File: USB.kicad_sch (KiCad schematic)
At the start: 4 parts, among them J6 USB_B_Micro, U1 MCP2221AxML

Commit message: generated drill and gerber files, updeted a few datasheets
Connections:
- net VBUS: now also J6.1 (VBUS), R3.1, U1.10 (VUSB), U1.16 (VDD)
- net at R3.2, U1.3 (~{RST}): no longer J6.1 (VBUS)
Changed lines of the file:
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@@
+	)
+	(junction
+		(at 121.92 91.44)
+		(diameter 0)
+		(color 0 0 0 0)
 	)
 	(junction
@@
 	)
 	(junction
-		(at 132.08 88.9)
+		(at 63.5 49.53)
 		(diameter 0)
 		(color 0 0 0 0)
@@
 	)
 	(junction
+		(at 146.05 60.96)
+		(diameter 0)
+		(color 0 0 0 0)
+	)
+	(junction
 		(at 63.5 59.69)
 		(diameter 0)
@@
 	(wire
 		(pts
-			(xy 132.08 88.9) (xy 132.08 91.44)
-		)
-		(stroke
-			(width 0)
-			(type default)
-		)
-	)
-	(wire
-		(pts
-			(xy 132.08 83.82) (xy 132.08 88.9)
-		)
-		(stroke
-			(width 0)
-			(type default)
-		)
-	)
-	(wire
-		(pts
 			(xy 63.5 71.12) (xy 63.5 68.58)
 		)
@@
 	(wire
 		(pts
-			(xy 63.5 59.69) (xy 63.5 49.53)
+			(xy 59.69 49.53) (xy 63.5 49.53)
+		)
+		(stroke
+			(width 0)
+			(type default)
+		)
+	)
+	(wire
+		(pts
+			(xy 137.16 60.96) (xy 137.16 95.25)
 		)
 		(stroke
@@
 	(wire
 		(pts
-			(xy 137.16 53.34) (xy 137.16 88.9)
-		)
-		(stroke
-			(width 0)
-			(type default)
-		)
-	)
-	(wire
-		(pts
 			(xy 109.22 73.66) (xy 104.14 73.66)
 		)
@@
 	(wire
 		(pts
+			(xy 137.16 95.25) (xy 121.92 95.25)
+		)
+		(stroke
+			(width 0)
+			(type default)
+		)
+	)
+	(wire
+		(pts
 			(xy 129.54 68.58) (xy 129.54 71.12)
 		)
@@
 	(wire
 		(pts
-			(xy 175.26 53.34) (xy 137.16 53.34)
+			(xy 175.26 60.96) (xy 146.05 60.96)
+		)
+		(stroke
+			(width 0)
+			(type default)
+		)
+	)
+	(wire
+		(pts
+			(xy 132.08 83.82) (xy 132.08 91.44)
+		)
+		(stroke
+			(width 0)
+			(type default)
+		)
+	)
+	(wire
+		(pts
+			(xy 121.92 95.25) (xy 121.92 91.44)
 		)
 		(stroke
@@
 	(wire
 		(pts
-			(xy 123.19 91.44) (xy 118.11 91.44)
+			(xy 123.19 91.44) (xy 121.92 91.44)
+		)
+		(stroke
+			(width 0)
+			(type default)
+		)
+	)
+	(wire
+		(pts
+			(xy 121.92 91.44) (xy 118.11 91.44)
 		)
 		(stroke
@@
 	(wire
 		(pts
+			(xy 66.04 49.53) (xy 63.5 49.53)
+		)
+		(stroke
+			(width 0)
+			(type default)
+		)
+	)
+	(wire
+		(pts
+			(xy 146.05 60.96) (xy 146.05 43.18)
+		)
+		(stroke
+			(width 0)
+			(type default)
+		)
+	)
+	(wire
+		(pts
 			(xy 64.77 67.31) (xy 64.77 69.85)
 		)
@@
 	(wire
 		(pts
-			(xy 175.26 53.34) (xy 175.26 60.96)
-		)
-		(stroke
-			(width 0)
-			(type default)
-		)
-	)
-	(wire
-		(pts
 			(xy 64.77 69.85) (xy 66.04 69.85)
 		)
@@
 	(wire
 		(pts
+			(xy 63.5 49.53) (xy 63.5 59.69)
+		)
+		(stroke
+			(width 0)
+			(type default)
+		)
+	)
+	(wire
+		(pts
 			(xy 63.5 67.31) (xy 64.77 67.31)
 		)
@@
 	(wire
 		(pts
-			(xy 137.16 88.9) (xy 132.08 88.9)
+			(xy 146.05 43.18) (xy 66.04 43.18)
 		)
 		(stroke
@@
 	(wire
 		(pts
+			(xy 146.05 60.96) (xy 137.16 60.96)
+		)
+		(stroke
+			(width 0)
+			(type default)
+		)
+	)
+	(wire
+		(pts
 			(xy 63.5 59.69) (xy 63.5 63.5)
+		)
+		(stroke
+			(width 0)
+			(type default)
+		)
+	)
+	(wire
+		(pts
+			(xy 66.04 43.18) (xy 66.04 49.53)
 		)
 		(stroke
@@
 	(hierarchical_label "VBUS"
 		(shape input)
-		(at 63.5 49.53 180)
+		(at 59.69 49.53 180)
 		(effects
 			(font

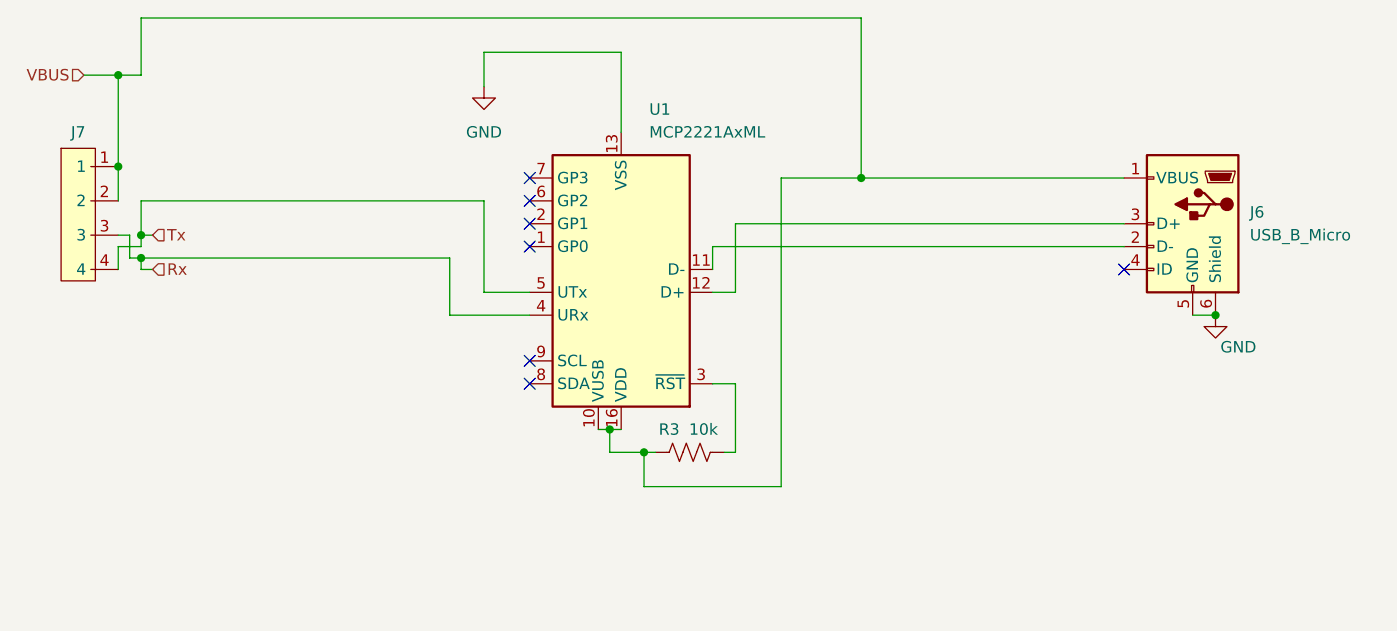
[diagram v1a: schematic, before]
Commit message: changed power supply of USB to UART to match datasheet, added changes to pcb Signed-off-by: Fozface <tyler.hickling99@gmail.com>
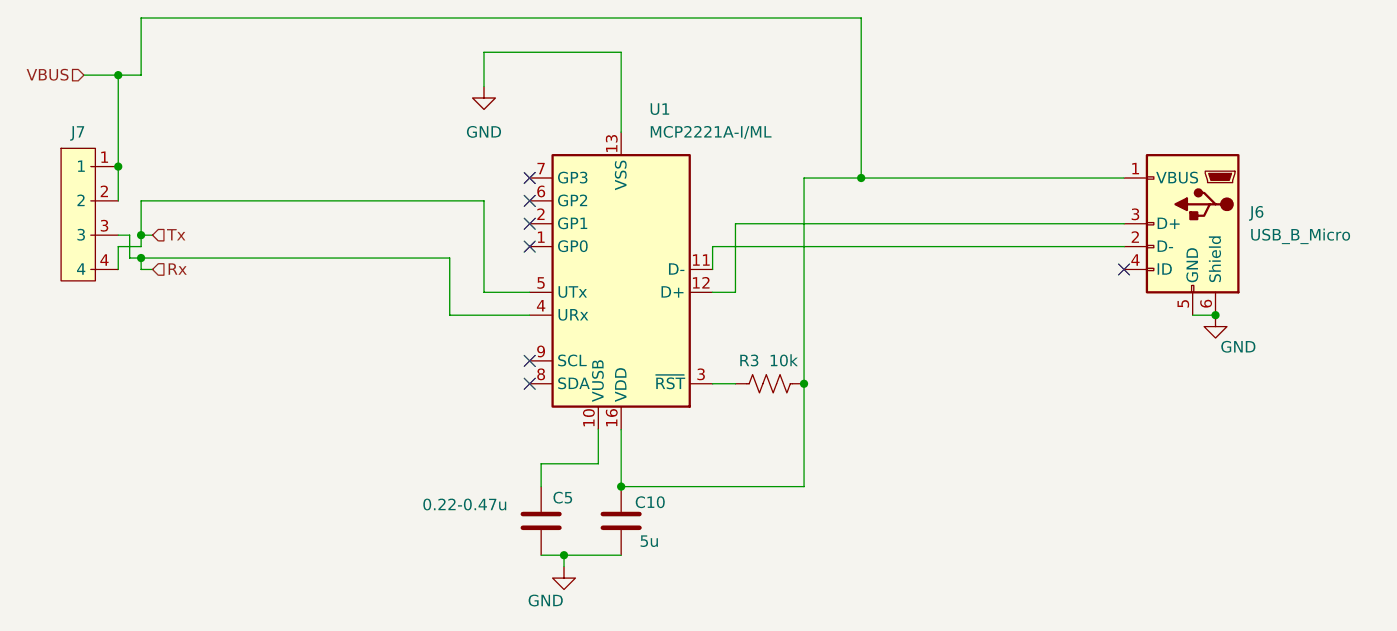
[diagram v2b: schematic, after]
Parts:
- added C10: 5u, Capacitor_SMD:C_1206_3216Metric_Pad1.33x1.80mm_HandSolder, symbol Device:C
- added C5: 0.22-0.47u, Capacitor_SMD:C_1206_3216Metric_Pad1.33x1.80mm_HandSolder, symbol Device:C
- U1: value MCP2221AxML -> MCP2221A-I/ML
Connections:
- net GND: now also C10.2, C5.2
- net VBUS: now also R3.2, C10.1; no longer R3.1, U1.10 (VUSB)
- net at U1.3 (~{RST}): now also R3.1; no longer R3.2
- new net: C5.1, U1.10 (VUSB)
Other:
- moved on the sheet: R3
